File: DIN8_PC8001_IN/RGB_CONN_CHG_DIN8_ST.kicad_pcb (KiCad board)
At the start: 2 copper layers, 16 x 16 mm, 9 parts, among them J1 DIGITAL, J2 TO_VGA1, J3 TO_VGA2

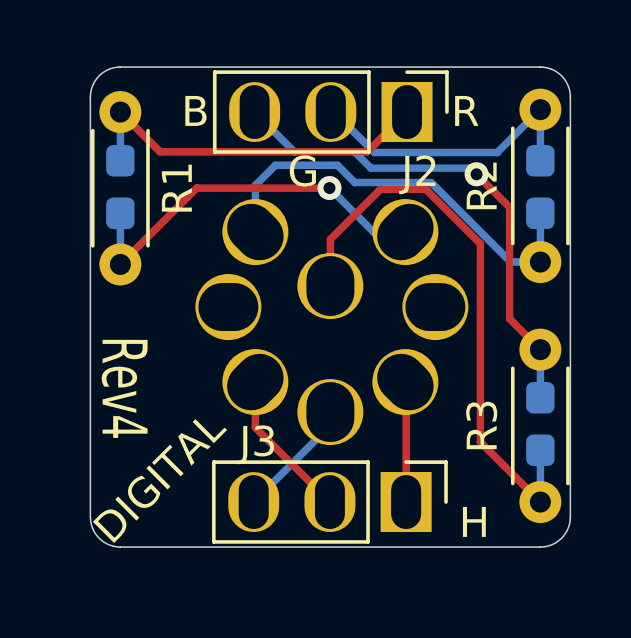
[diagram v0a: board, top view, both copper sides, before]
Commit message: update f_silk
added "Licensed under CERN-OHL-W v2"
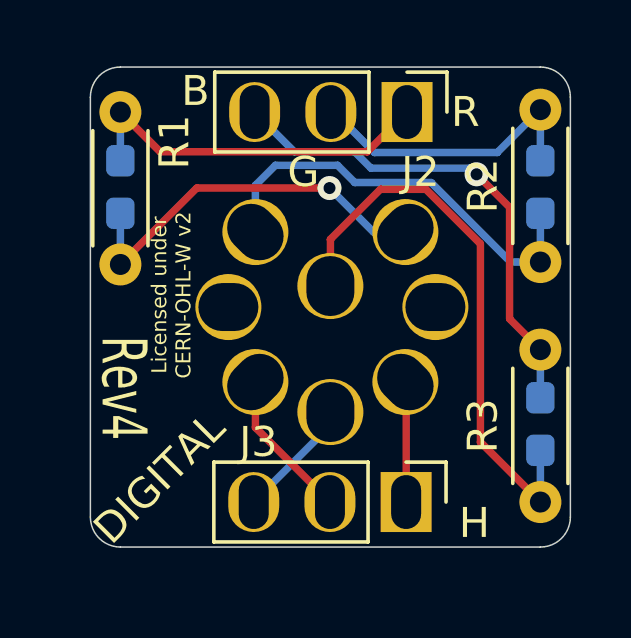
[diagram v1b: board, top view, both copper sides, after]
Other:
- board text added: "Licensed under CERN-OHL-W v2"
